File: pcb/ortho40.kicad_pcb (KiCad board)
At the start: 2 copper layers, 284 x 84 mm, 129 parts, among them J1 SWD, J2 USB_C_Receptacle_USB2.0, SW1 SW_Push, U1 RP2040, U2 XC6206PxxxMR, U3 W25Q128JVS, U4 USBLC6-2SC6, U5 ST7735S_1.8inch, Y1 12MHz

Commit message: Move some things
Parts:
- moved J1 9.06 mm to (167.0, 38.0)
- moved R1 8.25 mm to (169.0, 47.0)
- moved U5 1.00 mm to (180.0, 133.0)
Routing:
- net RESET: track 14.1 -> 5.20 mm
- net +3V3: track 56.2 -> 61.3 mm, vias 2 -> 4
- net GND: track 65.0 -> 69.9 mm
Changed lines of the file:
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@@
   )
   (footprint "Resistor_SMD:R_0402_1005Metric" (layer "B.Cu")
-    (at 171 55 -90)
+    (at 169 47 -90)
     (descr "Resistor SMD 0402 (1005 Metric), square (rectangular) end terminal, IPC_7351 nominal, (Body size source: IPC-SM-782 page 72, https://www.pcb-3d.com/wordpress/wp-content/uploads/ipc-sm-782a_amendment_1_and_2.pdf), generated with kicad-footprint-generator")
     (tags "resistor")
@@
   )
   (footprint "Connector_PinSocket_2.54mm:PinSocket_1x05_P2.54mm_Vertical" (layer "B.Cu")
-    (at 165.975 46.95 180)
+    (at 166.975 37.95 180)
     (descr "Through hole straight socket strip, 1x05, 2.54mm pitch, single row (from Kicad 4.0.7), script generated")
     (tags "Through hole socket strip THT 1x05 2.54mm single row")
@@
   )
   (footprint "Footprints:ST7735_1.8inch" (layer "B.Cu")
-    (at 180 134 90)
+    (at 180 133 90)
     (property "Sheetfile" "ortho40.kicad_sch")
     (property "Sheetname" "")
@@
   (segment (start 182 40) (end 183 39) (width 0.6) (layer "F.Cu") (net 1))
   (segment (start 180 42) (end 182 40) (width 0.6) (layer "F.Cu") (net 1))
+  (segment (start 174 51) (end 170 47) (width 0.381) (layer "F.Cu") (net 1))
   (segment (start 183 39) (end 185 39) (width 0.6) (layer "F.Cu") (net 1))
   (segment (start 180 43) (end 180 42) (width 0.6) (layer "F.Cu") (net 1))
+  (via (at 174 51) (size 0.6) (drill 0.3) (layers "F.Cu" "B.Cu") (net 1))
+  (via (at 170 47) (size 0.6) (drill 0.3) (layers "F.Cu" "B.Cu") (net 1))
   (via (at 185 39) (size 0.6) (drill 0.3) (layers "F.Cu" "B.Cu") (net 1))
   (via (at 180 43) (size 0.6) (drill 0.3) (layers "F.Cu" "B.Cu") (net 1))
@@
   (segment (start 172.52 42) (end 174 43.48) (width 0.6) (layer "B.Cu") (net 1))
   (segment (start 172.52 37.4825) (end 172.52 38.985) (width 0.6) (layer "B.Cu") (net 1))
+  (segment (start 169.49 46.49) (end 170 47) (width 0.381) (layer "B.Cu") (net 1))
   (segment (start 179.4 46.030025) (end 179.4 45.4) (width 0.2) (layer "B.Cu") (net 1))
   (segment (start 176.5625 47.4) (end 173.88 47.4) (width 0.2) (layer "B.Cu") (net 1))
@@
   (segment (start 183.4375 51) (end 182.624358 51) (width 0.2) (layer "B.Cu") (net 1))
   (segment (start 183.4375 51) (end 185 51) (width 0.2) (layer "B.Cu") (net 1))
+  (segment (start 169 46.49) (end 169.49 46.49) (width 0.381) (layer "B.Cu") (net 1))
   (segment (start 186.095 37.6) (end 186.095 37.905) (width 0.6) (layer "B.Cu") (net 1))
   (segment (start 179.8 45.8) (end 179.4 45.4) (width 0.2) (layer "B.Cu") (net 1))
@@
   (segment (start 179.8 47.096614) (end 180.067797 47.364411) (width 0.2) (layer "B.Cu") (net 1))
   (segment (start 179.4 46.5625) (end 179.4 46.030025) (width 0.2) (layer "B.Cu") (net 1))
+  (segment (start 167.895 46.49) (end 166.975 45.57) (width 0.381) (layer "B.Cu") (net 1))
+  (segment (start 169 46.49) (end 167.895 46.49) (width 0.381) (layer "B.Cu") (net 1))
   (segment (start 173.88 47.4) (end 173.48 47) (width 0.2) (layer "B.Cu") (net 1))
   (segment (start 182.624358 51) (end 182.426894 51.197464) (width 0.2) (layer "B.Cu") (net 1))
   (segment (start 174 43.48) (end 175 43.48) (width 0.6) (layer "B.Cu") (net 1))
   (segment (start 179.4 43.6) (end 179 43.2) (width 0.2) (layer "B.Cu") (net 1))
-  (segment (start 171 54.49) (end 172.37267 54.49) (width 0.2) (layer "B.Cu") (net 1))
+  (segment (start 174 51.321178) (end 174 51) (width 0.381) (layer "B.Cu") (net 1))
   (segment (start 177.4 45.88) (end 175 43.48) (width 0.2) (layer "B.Cu") (net 1))
   (segment (start 176.5625 51) (end 177.203344 51) (width 0.2) (layer "B.Cu") (net 1))
@@
   (segment (start 179 43.2) (end 179 42.48) (width 0.2) (layer "B.Cu") (net 1))
   (segment (start 174.339411 51.660589) (end 175 51) (width 0.2) (layer "B.Cu") (net 1))
-  (segment (start 174.339411 52.523259) (end 174.339411 51.660589) (width 0.2) (layer "B.Cu") (net 1))
+  (segment (start 174.339411 51.660589) (end 174 51.321178) (width 0.381) (layer "B.Cu") (net 1))
   (segment (start 179.8 55.2) (end 179.339411 55.660589) (width 0.2) (layer "B.Cu") (net 1))
   (segment (start 175 51) (end 176.5625 51) (width 0.2) (layer "B.Cu") (net 1))
@@
   (segment (start 177.4 46.5625) (end 177.4 47.4) (width 0.2) (layer "B.Cu") (net 1))
   (segment (start 173.48 45) (end 173.48 47) (width 0.381) (layer "B.Cu") (net 1))
-  (segment (start 172.37267 54.49) (end 174.339411 52.523259) (width 0.2) (layer "B.Cu") (net 1))
   (segment (start 172.52 40) (end 172.52 42) (width 0.6) (layer "B.Cu") (net 1))
   (segment (start 178.725 48.725) (end 180 48.725) (width 0.635) (layer "F.Cu") (net 2))
@@
   (segment (start 181.876058 41.123942) (end 182.573112 41.123942) (width 0.381) (layer "B.Cu") (net 2))
   (segment (start 176.455282 42.540759) (end 175.540759 42.540759) (width 0.381) (layer "B.Cu") (net 2))
+  (segment (start 171 45) (end 169.03 43.03) (width 0.381) (layer "B.Cu") (net 2))
   (segment (start 181 29.660618) (end 181.660618 29) (width 0.381) (layer "B.Cu") (net 2))
   (segment (start 175.660589 57.339411) (end 175 58) (width 0.381) (layer "B.Cu") (net 2))
@@
   (segment (start 180.27 61.48) (end 180.9 60.85) (width 0.25) (layer "B.Cu") (net 2))
   (segment (start 172 32) (end 173.52 32) (width 0.6) (layer "B.Cu") (net 2))
+  (segment (start 169.03 43.03) (end 166.975 43.03) (width 0.381) (layer "B.Cu") (net 2))
   (segment (start 184 28.51) (end 184 29.100695) (width 0.381) (layer "B.Cu") (net 2))
   (segment (start 179 41.52) (end 179.02 41.5) (width 0.381) (layer "B.Cu") (net 2))
@@
   (segment (start 176 27.6) (end 177.55 26.05) (width 0.6) (layer "B.Cu") (net 58))
   (segment (start 182.374499 22.374499) (end 182.374499 23.969499) (width 0.381) (layer "B.Cu") (net 58))
-  (segment (start 169.4 57.11) (end 165.975 57.11) (width 0.2) (layer "B.Cu") (net 61))
-  (segment (start 171 55.51) (end 169.4 57.11) (width 0.2) (layer "B.Cu") (net 61))
-  (segment (start 171 55.51) (end 176.49 55.51) (width 0.2) (layer "B.Cu") (net 61))
+  (segment (start 168.4 48.11) (end 166.975 48.11) (width 0.2) (layer "B.Cu") (net 61))
   (segment (start 177.256346 55) (end 178.2 54.056346) (width 0.2) (layer "B.Cu") (net 61))
   (segment (start 176.49 55.51) (end 177 55) (width 0.2) (layer "B.Cu") (net 61))
   (segment (start 177 55) (end 177.256346 55) (width 0.2) (layer "B.Cu") (net 61))
+  (segment (start 169 47.51) (end 168.4 48.11) (width 0.2) (layer "B.Cu") (net 61))
   (segment (start 178.2 53.4375) (end 178.2 54.056346) (width 0.2) (layer "B.Cu") (net 61))
   (segment (start 178.75 26.74) (end 178 27.49) (width 0.25) (layer "B.Cu") (net 62))
@@
     )
   )
-  (zone (net 2) (net_name "GND") (layer "B.Cu") (hatch edge 0.508)
+  (zone (net 2) (net_name "GND") (layer "B.Cu") (name "GND") (hatch edge 0.508)
     (connect_pads (clearance 0.508))
     (min_thickness 0.254) (filled_areas_thickness no)

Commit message: Fully finish PCB
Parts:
- moved U5 79.0 mm to (181.0, 54.0)
- moved J1 33.7 mm to (182.1, 68.0), turned to 90 degrees
- moved R1 18.2 mm to (172.0, 65.0), turned to 180 degrees
- moved C13 3.61 mm to (171.0, 54.0)
- moved C11 2.00 mm to (188.0, 52.0)
- moved C15 1.95 mm to (186.0, 62.0)
- moved C16 1.95 mm to (178.0, 63.0)
- moved R7 1.95 mm to (181.0, 59.0)
- moved Y1 1.95 mm to (182.0, 62.0)
- moved C1 1.93 mm to (179.1, 57.9), turned to -120 degrees
- moved C4 1.57 mm to (177.5, 57.5)
- moved C10 1.14 mm to (172.5, 46.0)
- moved C8 1.14 mm to (172.5, 44.0)
- renumbered Ce to C4
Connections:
- U1 pad 13: unconnected-(U1-Pad13) -> r2
- U1 pad 14: unconnected-(U1-Pad14) -> r3
- U1 pad 2: unconnected-(U1-Pad2) -> c6
- U1 pad 3: unconnected-(U1-Pad3) -> c7
- U1 pad 34: unconnected-(U1-Pad34) -> c0
- U1 pad 35: unconnected-(U1-Pad35) -> c1
- U1 pad 36: unconnected-(U1-Pad36) -> c2
- U1 pad 37: unconnected-(U1-Pad37) -> c3
- U1 pad 38: unconnected-(U1-Pad38) -> c4
- U1 pad 39: unconnected-(U1-Pad39) -> c5
- U1 pad 4: unconnected-(U1-Pad4) -> c8
- U1 pad 40: unconnected-(U1-Pad40) -> r1
- U1 pad 41: unconnected-(U1-Pad41) -> r0
- U1 pad 5: unconnected-(U1-Pad5) -> c9
- U1 pad 6: unconnected-(U1-Pad6) -> c10
- U1 pad 7: unconnected-(U1-Pad7) -> c11
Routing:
- net c11: track 0.00 -> 189.0 mm, vias 0 -> 1
- net c10: track 0.00 -> 168.8 mm, vias 0 -> 1
- net c9: track 0.00 -> 148.6 mm, vias 0 -> 1
- net c0: track 60.0 -> 196.4 mm, vias 0 -> 1
- net c8: track 0.00 -> 128.5 mm, vias 0 -> 1
- net c1: track 60.0 -> 175.8 mm, vias 0 -> 1
- net c7: track 0.00 -> 108.3 mm, vias 0 -> 1
- net c2: track 60.0 -> 155.1 mm, vias 0 -> 1
- net c6: track 0.00 -> 88.1 mm, vias 0 -> 1
- net c3: track 60.0 -> 134.4 mm, vias 0 -> 1
- net r1: track 258.5 -> 327.6 mm
- net c4: track 60.0 -> 113.8 mm, vias 0 -> 1
- net r3: track 290.3 -> 342.2 mm
- net c5: track 60.0 -> 107.3 mm, vias 0 -> 1
- net r2: track 281.0 -> 313.0 mm
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
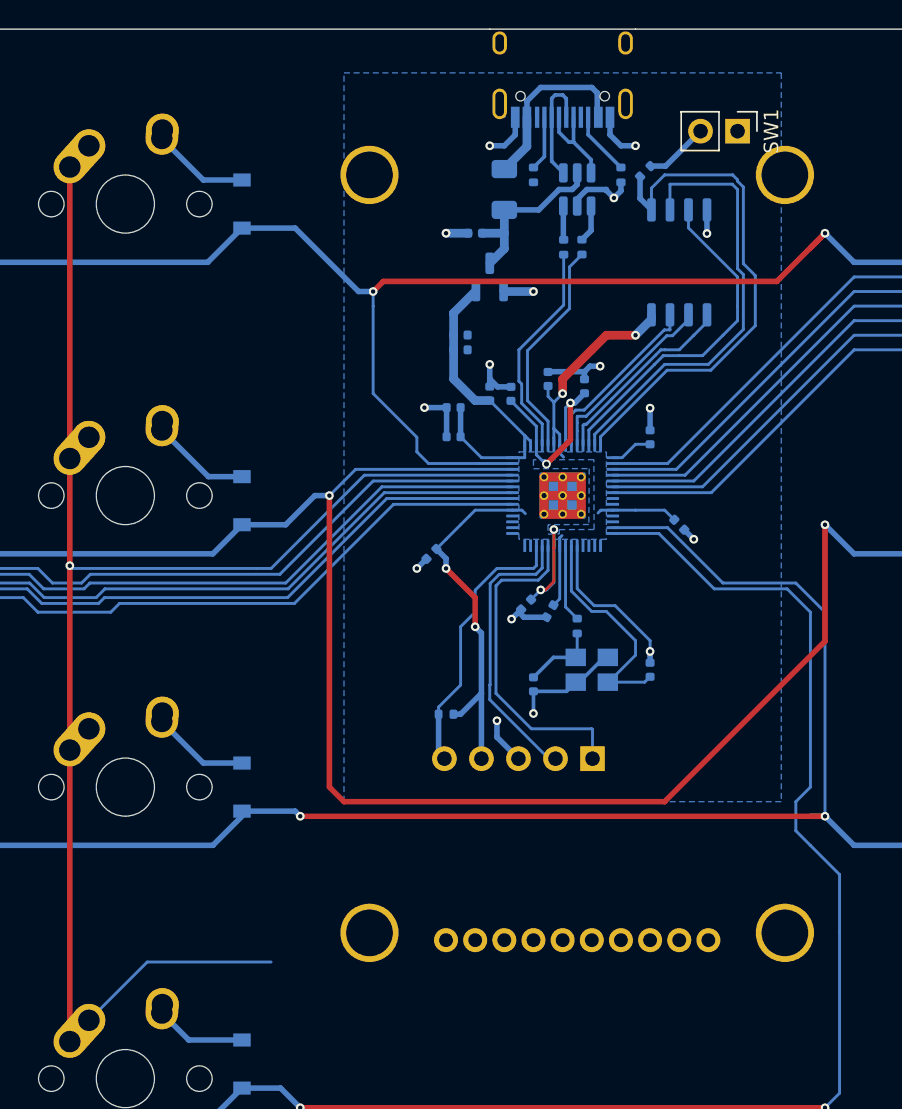
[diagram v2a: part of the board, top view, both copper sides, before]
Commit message: Setup Display
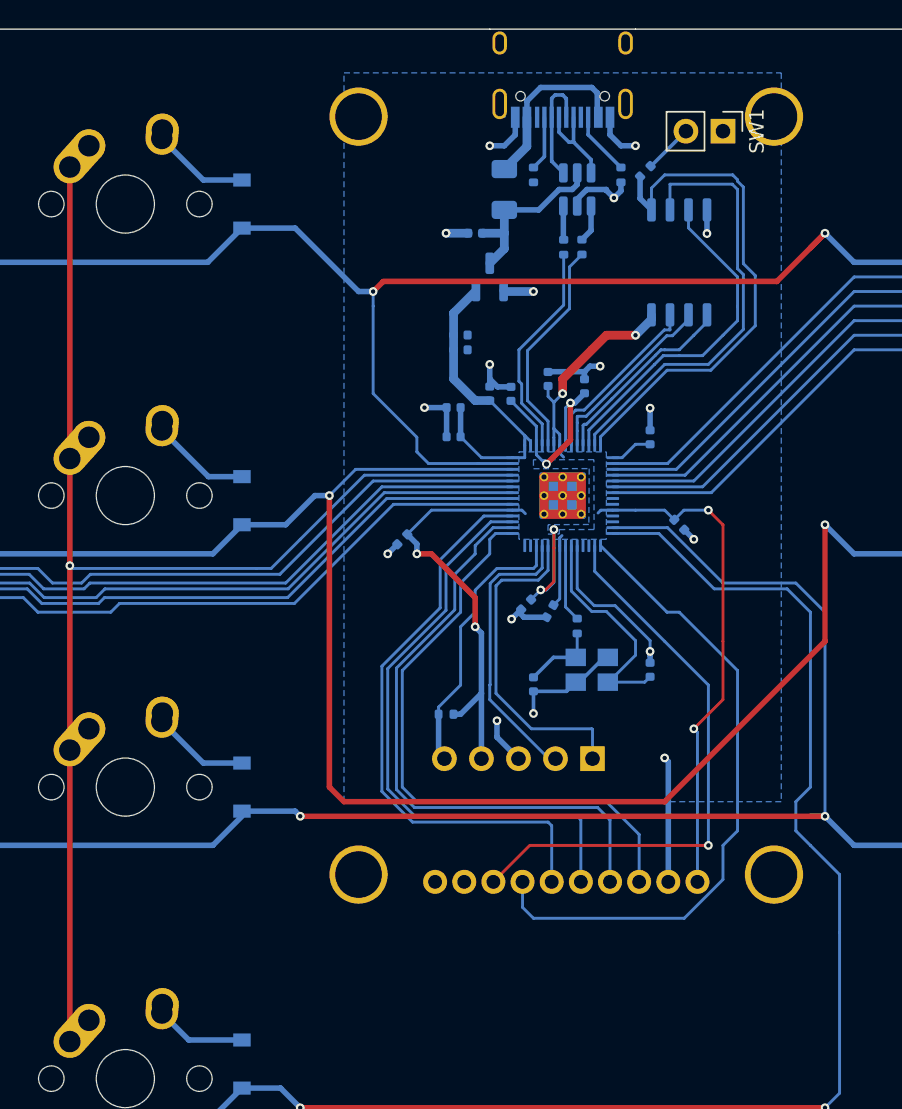
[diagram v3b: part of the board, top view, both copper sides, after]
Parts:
- moved U5 4.07 mm to (180.2, 50.0)
- moved C13 2.24 mm to (169.0, 53.0)
- moved SW1 1.00 mm to (191.0, 25.0)
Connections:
- U1 pad 15: unconnected-(U1-Pad15) -> LCD_RESET
- U1 pad 16: unconnected-(U1-Pad16) -> LCD_DC
- U1 pad 29: unconnected-(U1-Pad29) -> LCD_SCK
- U1 pad 30: unconnected-(U1-Pad30) -> LCD_TX
- U1 pad 31: unconnected-(U1-Pad31) -> LCD_RX
- U1 pad 32: unconnected-(U1-Pad32) -> LCD_CS
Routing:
- net LCD_RESET: track 0.00 -> 44.6 mm
- net LCD_SCK: track 0.00 -> 42.1 mm
- net LCD_TX: track 0.00 -> 41.8 mm
- net LCD_RX: track 0.00 -> 41.1 mm
- net LCD_CS: track 0.00 -> 40.2 mm
- net LCD_DC: track 0.00 -> 39.6 mm, vias 0 -> 1
- net +3V3: track 77.9 -> 111.4 mm, vias 4 -> 6
- net c5: track 107.3 -> 93.1 mm
- net GND: track 72.3 -> 80.9 mm, vias 16 -> 17
- net /~{BOOTSEL}: track 4.42 -> 3.42 mm

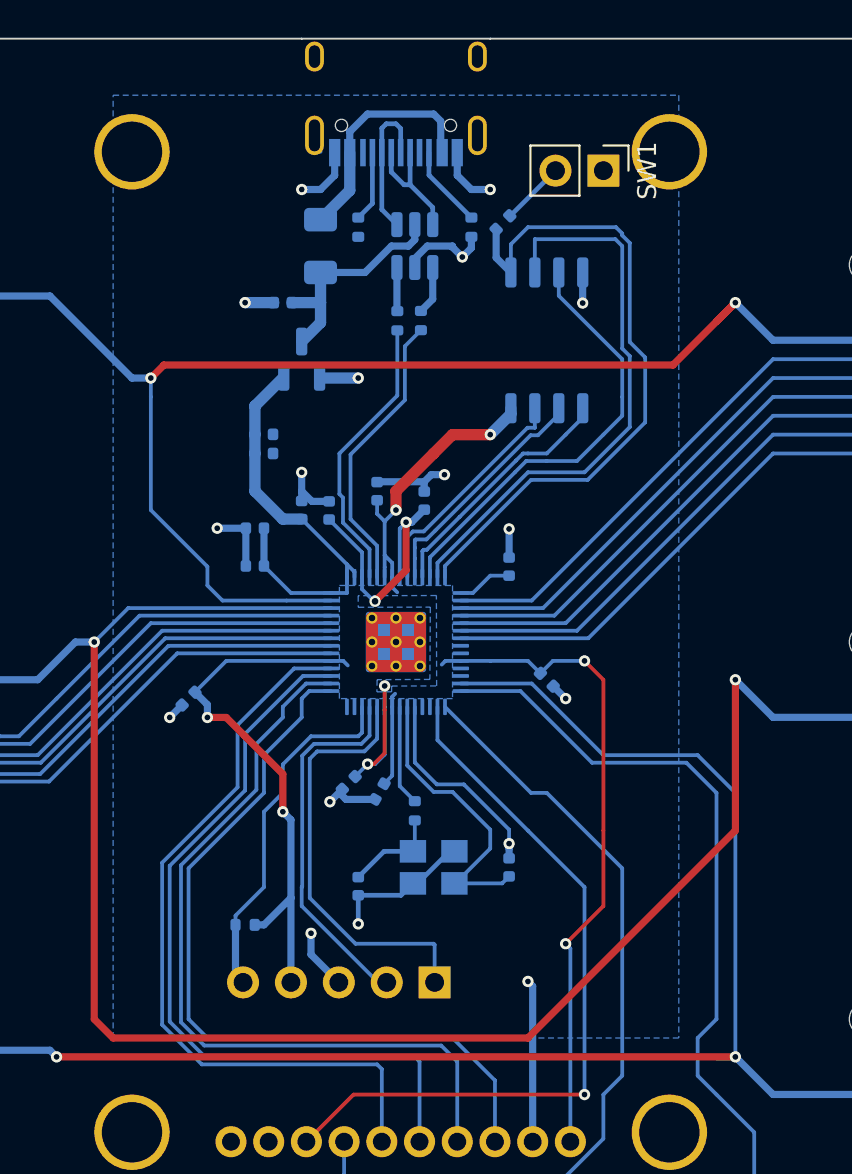
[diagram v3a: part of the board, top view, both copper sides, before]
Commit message: Possibly fix nets?
I'm not sure but the top pin for +3v3 is still funky :(
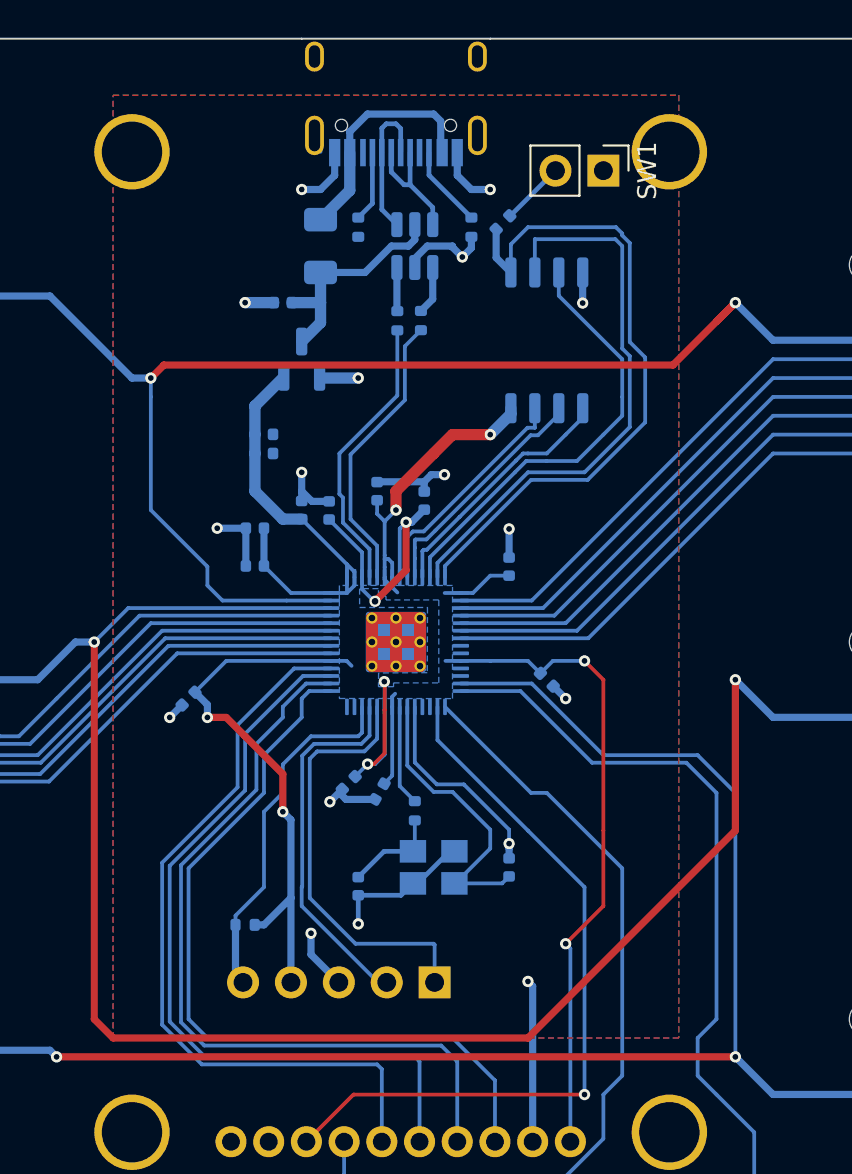
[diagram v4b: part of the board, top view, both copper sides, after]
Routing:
- net +3V3: track 111.4 -> 113.9 mm
- net r2: track 313.0 -> 312.0 mm
- added copper zone on F.Cu, net GND
